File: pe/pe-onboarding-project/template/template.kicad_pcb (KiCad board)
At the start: 2 copper layers, 0 parts

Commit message: Add files via upload
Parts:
- added C1: 22uF, Capacitor_SMD:C_0805_2012Metric, F.Cu at (123.0, 108.5)
- added C2: 22uF, Capacitor_SMD:C_0805_2012Metric, F.Cu at (126.0, 108.5)
- added C3: 22uF, Capacitor_SMD:C_0805_2012Metric, F.Cu at (129.0, 108.5)
- added C4: 22uF, Capacitor_SMD:C_0805_2012Metric, F.Cu at (132.0, 108.5)
- added C5: 22uF, Capacitor_SMD:C_0805_2012Metric, F.Cu at (135.0, 108.5)
- added CBoot1: 0.1 µF, Capacitor_SMD:C_0603_1608Metric, F.Cu at (141.0, 105.5)
- added CO1: 22 µF, Capacitor_SMD:C_0603_1608Metric, F.Cu at (125.0, 104.7)
- added CO2: 22 µF, Capacitor_SMD:C_0603_1608Metric, F.Cu at (127.5, 104.7)
- added CO3: 22 µF, Capacitor_SMD:C_0603_1608Metric, F.Cu at (130.0, 104.7)
- added CO4: 22 µF, Capacitor_SMD:C_0603_1608Metric, F.Cu at (132.5, 104.7)
- added CO5: 0.1 µF, Capacitor_SMD:C_0603_1608Metric, F.Cu at (135.0, 104.7)
- added L1: 4.7uH, FSCustom:IND_BOURNS_SRN6045, F.Cu at (141.5, 100.3)
- added R1: 54.9 kΩ, Resistor_SMD:R_0603_1608Metric, F.Cu at (148.0, 110.8)
- added R2: 10 kΩ, Resistor_SMD:R_0603_1608Metric, F.Cu at (145.5, 110.8)
- added U2: TPS562208DDCR, FSCustom:DDC0006A_N, F.Cu at (141.0, 108.5)
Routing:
- net GND: track 0.00 -> 58.9 mm
- net /VOUT: track 0.00 -> 37.7 mm
- net /VIN: track 0.00 -> 16.7 mm
- net Net-(U2-SW): track 0.00 -> 7.96 mm
- net Net-(U2-VFB): track 0.00 -> 5.85 mm
- net Net-(U2-VBST): track 0.00 -> 2.30 mm
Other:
- board outline added: 31 x 19 mm

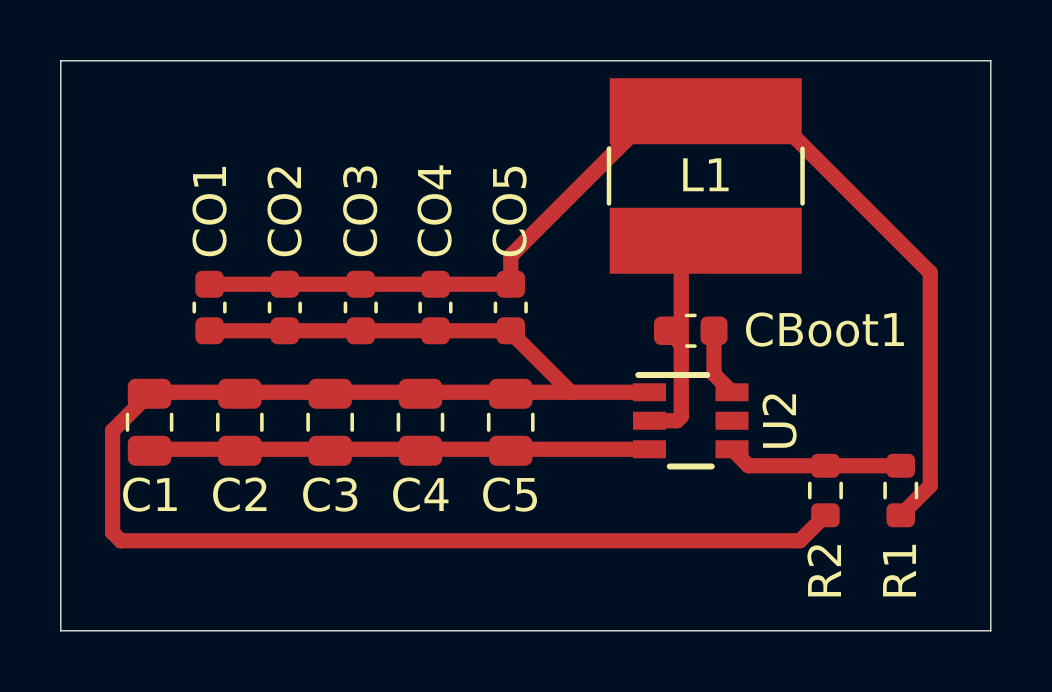
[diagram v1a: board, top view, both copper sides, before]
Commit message: Update to PCB Design
Removed the wiring cross over by using the background copper layer.
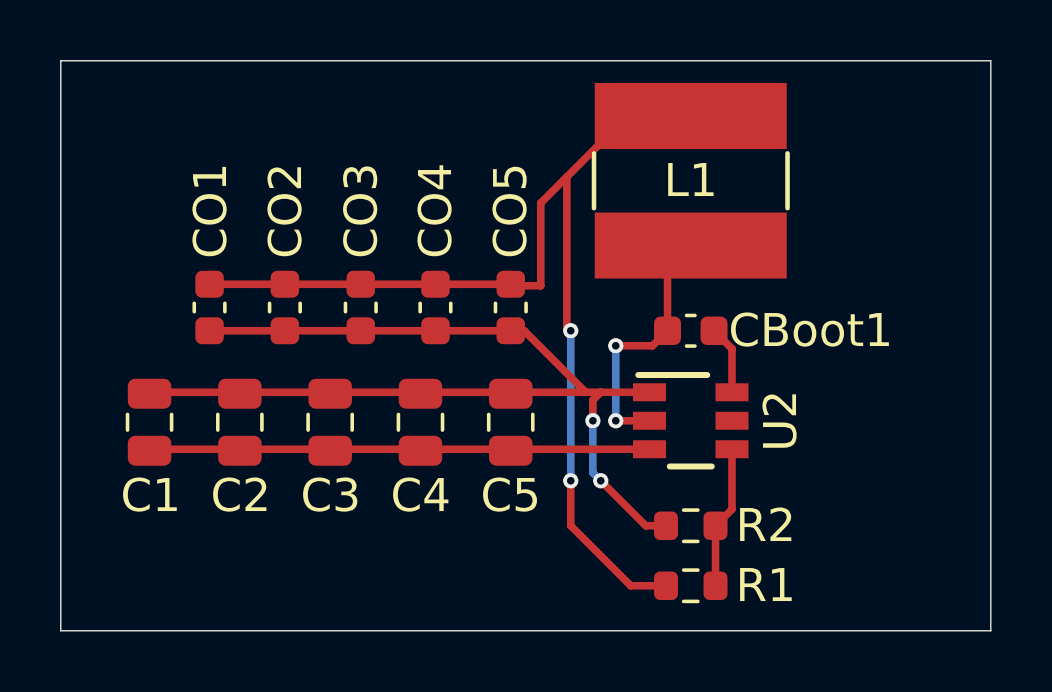
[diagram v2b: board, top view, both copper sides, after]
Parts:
- moved R1 7.69 mm to (141.0, 114.0), turned to 180 degrees
- moved R2 4.64 mm to (141.0, 112.0), turned to 180 degrees
- moved L1 0.52 mm to (141.0, 100.5)
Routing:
- net GND: track 58.9 -> 36.0 mm, vias 0 -> 2
- net /VOUT: track 37.7 -> 35.7 mm, vias 0 -> 2
- net Net-(U2-VFB): track 5.85 -> 4.78 mm
- net Net-(U2-SW): track 7.96 -> 8.72 mm, vias 0 -> 2
